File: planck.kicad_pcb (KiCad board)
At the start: 2 copper layers, 53 parts, among them J1 USB_C_Receptacle_USB2.0, K1 KEYSW, K2 KEYSW, K3 KEYSW, K4 KEYSW, SW1 SW_PUSH, U1 ATmega32U4-M, Y1 Crystal_GND24_Small

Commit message: poured fills
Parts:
- J1, K1, K2, K3, K4, TP1, TP2: moved to B.Cu
- TP10: value TestPoint -> PB5; moved to B.Cu
- TP11: value TestPoint -> PB6; moved to B.Cu
- TP12: value TestPoint -> PB7; moved to B.Cu
- TP13: value TestPoint -> PC6; moved to B.Cu
- TP14: value TestPoint -> PC7; moved to B.Cu
- TP15: value TestPoint -> PD0; moved to B.Cu
- TP16: value TestPoint -> PD1; moved to B.Cu
- TP17: value TestPoint -> PD2; moved to B.Cu
- TP18: value TestPoint -> PD3; moved to B.Cu
- TP19: value TestPoint -> PD4; moved to B.Cu
- TP20: value TestPoint -> PD6; moved to B.Cu
- TP21: value TestPoint -> PD7; moved to B.Cu
- TP22: value TestPoint -> PE6; moved to B.Cu
- TP23: value TestPoint -> PF6; moved to B.Cu
- TP24: value TestPoint -> PF7; moved to B.Cu
- TP3: value TestPoint -> AREF; moved to B.Cu
- TP4: value TestPoint -> PD5; moved to B.Cu
- TP5: value TestPoint -> PB0; moved to B.Cu
- TP6: value TestPoint -> PB1; moved to B.Cu
- TP7: value TestPoint -> PB2; moved to B.Cu
- TP8: value TestPoint -> PB3; moved to B.Cu
- TP9: value TestPoint -> PB4; moved to B.Cu
- moved D2 68.3 mm to (107.2, 132.6)
- moved K1 63.7 mm to (84.8, 101.8), turned to 180 degrees
- moved K4 63.4 mm to (104.1, 101.8), turned to 180 degrees
- moved K3 62.9 mm to (84.8, 121.2), turned to 180 degrees
- moved K2 62.6 mm to (104.1, 121.2), turned to 180 degrees
- moved D6 62.1 mm to (107.2, 111.8)
- moved C1 61.5 mm to (90.9, 95.0), turned to 90 degrees
- moved D5 60.0 mm to (86.9, 132.1)
- moved R4 57.9 mm to (107.7, 95.0), turned to 90 degrees
- moved TP13 56.1 mm to (94.5, 87.4), turned to 180 degrees
- moved TP1 55.2 mm to (99.6, 87.4), turned to 180 degrees
- moved TP23 53.6 mm to (86.9, 87.4), turned to 180 degrees
- moved C8 51.8 mm to (82.8, 81.8)
- moved SW1 51.3 mm to (84.8, 86.4)
- moved TP8 50.0 mm to (94.5, 83.3), turned to 180 degrees
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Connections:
- net /reset renamed /~{reset}
- net Net-(TP10-Pad1) renamed /PB5
- net Net-(TP11-Pad1) renamed /PB6
- net Net-(TP12-Pad1) renamed /PB7
- net Net-(TP13-Pad1) renamed /PC6
- net Net-(TP14-Pad1) renamed /PC7
- net Net-(TP15-Pad1) renamed /PD0
- net Net-(TP16-Pad1) renamed /PD1
- net Net-(TP17-Pad1) renamed /PD2
- net Net-(TP18-Pad1) renamed /PD3
- net Net-(TP19-Pad1) renamed /PD4
- net Net-(TP20-Pad1) renamed /PD6
- net Net-(TP21-Pad1) renamed /PD7
- net Net-(TP22-Pad1) renamed /PE6
- net Net-(TP23-Pad1) renamed /PF6
- net Net-(TP24-Pad1) renamed /PF7
- net Net-(TP4-Pad1) renamed /PD5
- net Net-(TP5-Pad1) renamed /PB0
- net Net-(TP6-Pad1) renamed /PB1
- net Net-(TP7-Pad1) renamed /PB2
- net Net-(TP8-Pad1) renamed /PB3
- net Net-(TP9-Pad1) renamed /PB4
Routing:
- added copper zone on B.Cu, net GND
- added copper zone on F.Cu, net GND
- added copper zone on In1.Cu, net GND
- added copper zone on In2.Cu, net VCC
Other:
- board outline added: 39.4 x 58.4 mm
- copper layers 2 -> 4

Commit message: started routing
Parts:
- moved R3 7.81 mm to (113.0, 95.5), turned to 0 degrees
- moved D4 7.44 mm to (113.5, 92.4), turned to 180 degrees
- moved D3 3.50 mm to (108.9, 92.5), turned to 0 degrees
- moved D2 1.85 mm to (106.7, 130.8)
- moved D5 1.48 mm to (87.6, 130.8)
- moved C7 1.14 mm to (81.4, 93.4)
- moved C9 1.10 mm to (87.2, 93.5)
- moved D1 0.76 mm to (87.4, 111.3)
- moved D6 0.72 mm to (106.7, 111.3)
- moved R4 0.30 mm to (107.9, 95.2), turned to 0 degrees
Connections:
- net /~{reset} renamed /~{{reset}}
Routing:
- net /col0: track 0.00 -> 27.8 mm
- net /col1: track 0.00 -> 27.3 mm
- net /row0: track 0.00 -> 21.6 mm
- net /row1: track 0.00 -> 21.5 mm
- net Net-(D4-Pad1): track 0.00 -> 8.57 mm, vias 0 -> 1
- net Net-(D2-Pad2): track 0.00 -> 8.01 mm
- net Net-(D5-Pad2): track 0.00 -> 7.90 mm
- net Net-(D1-Pad2): track 0.00 -> 7.80 mm
- net Net-(D6-Pad2): track 0.00 -> 7.80 mm
- net Net-(D3-Pad1): track 0.00 -> 5.63 mm

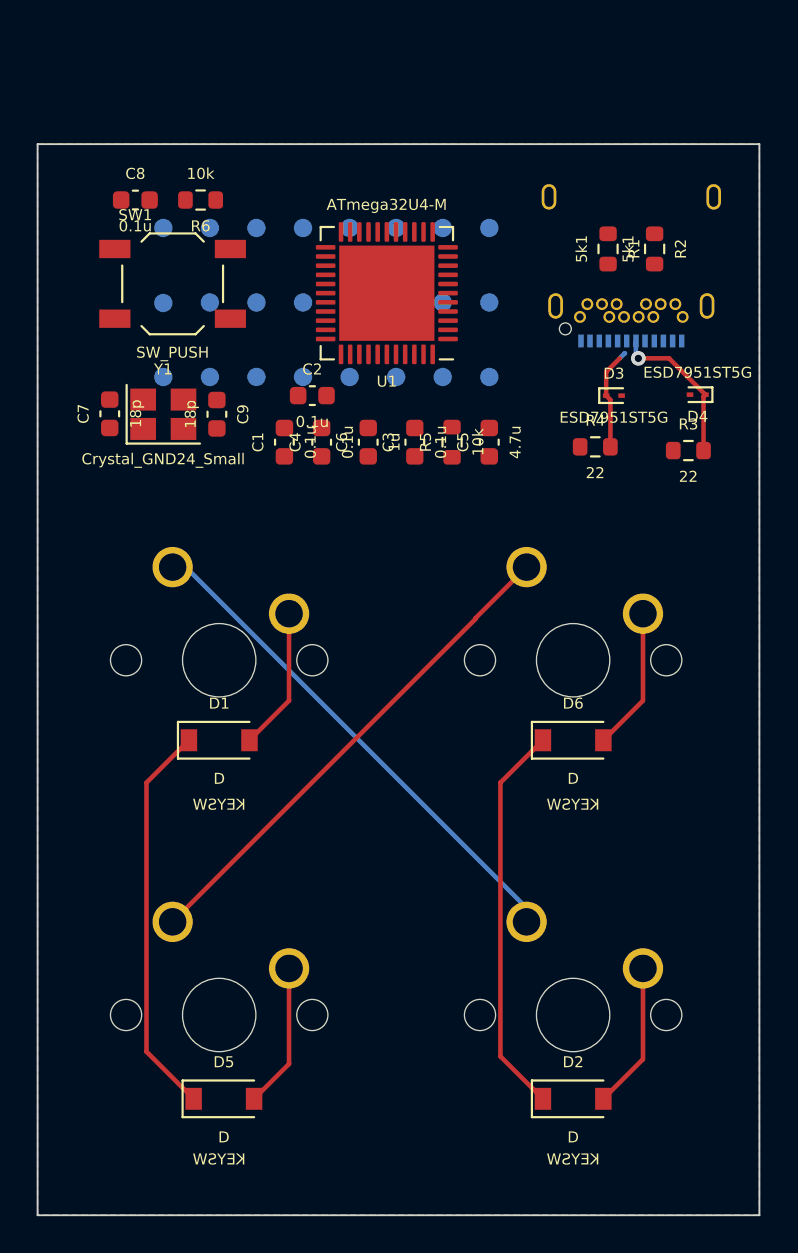
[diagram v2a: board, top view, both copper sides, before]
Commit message: routed crystal
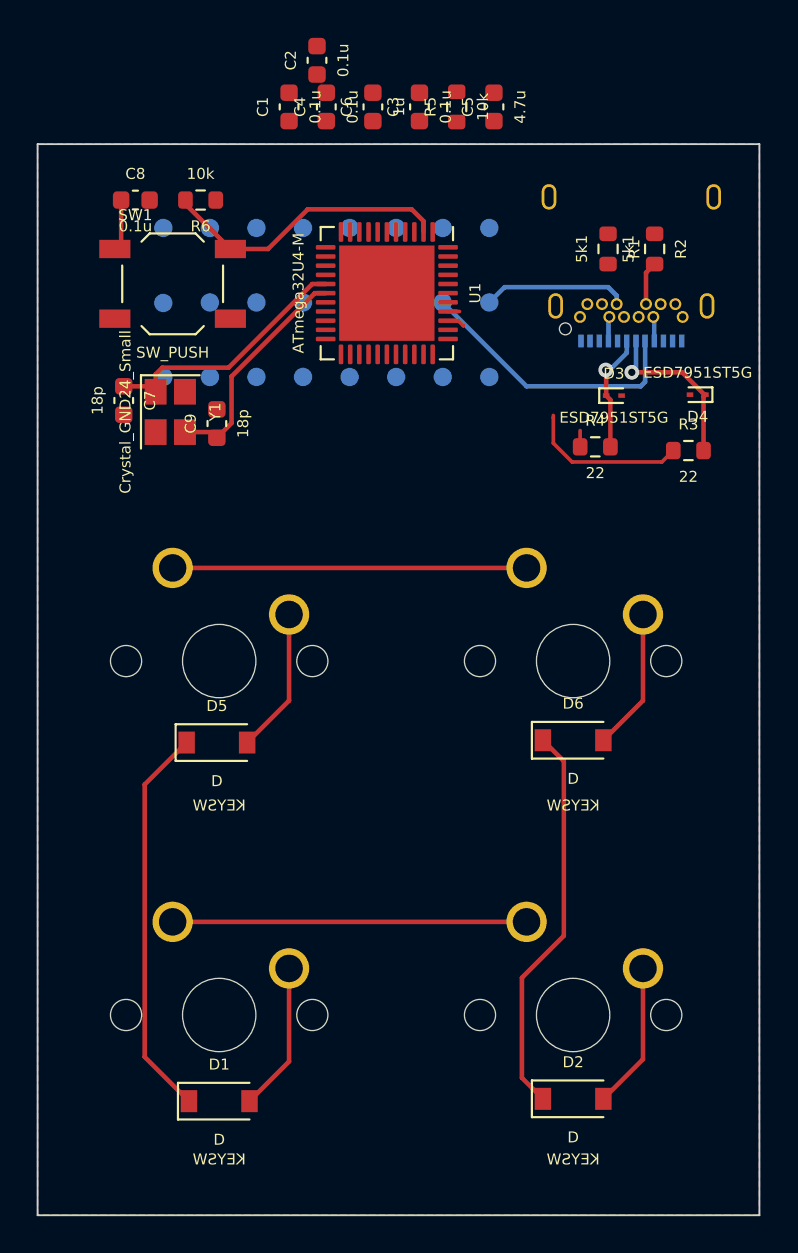
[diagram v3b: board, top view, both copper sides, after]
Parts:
- moved D1 19.7 mm to (87.4, 130.9)
- moved D5 19.4 mm to (87.2, 111.4)
- moved K1 19.3 mm to (84.8, 121.2)
- moved K3 19.3 mm to (84.8, 101.9)
- moved C1 18.3 mm to (91.2, 76.7)
- moved C2 18.3 mm to (92.7, 74.2), turned to 90 degrees
- moved C3 18.3 mm to (98.3, 76.7)
- moved C4 18.3 mm to (93.2, 76.7)
- moved C5 18.3 mm to (102.4, 76.7)
- moved C6 18.3 mm to (95.8, 76.7)
- moved R5 18.3 mm to (100.3, 76.7)
- moved TP2 5.08 mm to (102.1, 87.4)
- moved TP3 5.08 mm to (97.0, 87.4), turned to -90 degrees
- moved C7 1.05 mm to (82.2, 92.7), turned to -90 degrees
- moved C9 0.51 mm to (87.2, 94.0), turned to 90 degrees
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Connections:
- net /~{{reset}} renamed /~reset
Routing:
- net /~reset: track 0.00 -> 18.8 mm
- net Net-(J1-PadA8): track 0.00 -> 15.3 mm
- net /XTAL2: track 0.00 -> 14.2 mm
- net /XTAL1: track 0.00 -> 12.6 mm
- net /D-: track 0.00 -> 8.74 mm
- net Net-(J1-PadB8): track 0.00 -> 7.95 mm
- net /col0: track 27.8 -> 20.1 mm
- net /col1: track 27.3 -> 20.0 mm
- net VCC: track 0.00 -> 2.66 mm
- net Net-(J1-PadB5): track 0.00 -> 2.38 mm
- net /PF7: track 0.00 -> 0.97 mm
- net /D+: track 0.00 -> 0.89 mm
- net Net-(D3-Pad1): track 5.63 -> 6.48 mm, vias 0 -> 1
- net Net-(D4-Pad1): track 8.57 -> 9.41 mm
- net /PF6: track 0.00 -> 0.63 mm

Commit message: finishing it off
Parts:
- removed TP10: PB5, TestPoint:TestPoint_Pad_D1.0mm
- removed TP11: PB6, TestPoint:TestPoint_Pad_D1.0mm
- removed TP12: PB7, TestPoint:TestPoint_Pad_D1.0mm
- removed TP13: PC6, TestPoint:TestPoint_Pad_D1.0mm
- removed TP14: PC7, TestPoint:TestPoint_Pad_D1.0mm
- removed TP15: PD0, TestPoint:TestPoint_Pad_D1.0mm
- removed TP16: PD1, TestPoint:TestPoint_Pad_D1.0mm
- removed TP17: PD2, TestPoint:TestPoint_Pad_D1.0mm
- removed TP18: PD3, TestPoint:TestPoint_Pad_D1.0mm
- removed TP19: PD4, TestPoint:TestPoint_Pad_D1.0mm
- removed TP20: PD6, TestPoint:TestPoint_Pad_D1.0mm
- removed TP21: PD7, TestPoint:TestPoint_Pad_D1.0mm
- removed TP22: PE6, TestPoint:TestPoint_Pad_D1.0mm
- removed TP23: PF6, TestPoint:TestPoint_Pad_D1.0mm
- removed TP24: PF7, TestPoint:TestPoint_Pad_D1.0mm
- removed TP4: PD5, TestPoint:TestPoint_Pad_D1.0mm
- removed TP5: PB0, TestPoint:TestPoint_Pad_D1.0mm
- removed TP6: PB1, TestPoint:TestPoint_Pad_D1.0mm
- removed TP7: PB2, TestPoint:TestPoint_Pad_D1.0mm
- removed TP8: PB3, TestPoint:TestPoint_Pad_D1.0mm
- removed TP9: PB4, TestPoint:TestPoint_Pad_D1.0mm
- moved TP3 31.4 mm to (121.4, 67.6)
- moved TP1 29.0 mm to (123.4, 70.9)
- moved TP2 29.0 mm to (126.0, 70.9)
- moved R5 25.7 mm to (80.2, 92.6), turned to 180 degrees
- moved C7 24.0 mm to (63.5, 77.6)
- moved C9 24.0 mm to (68.6, 78.9)
- moved Y1 24.0 mm to (66.0, 78.2)
- moved C3 20.4 mm to (89.2, 94.9), turned to -90 degrees
- moved C1 20.2 mm to (82.4, 94.9), turned to -90 degrees
- moved C2 17.1 mm to (80.2, 85.9), turned to 180 degrees
- moved SW1 16.7 mm to (96.8, 74.7), turned to 90 degrees
- moved C5 16.5 mm to (87.3, 83.5)
- moved C4 14.6 mm to (91.5, 91.2), turned to 0 degrees
- moved C6 13.2 mm to (91.5, 89.2), turned to 0 degrees
- moved U1 10.9 mm to (85.8, 89.2), turned to 180 degrees
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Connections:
- U1 pad 1: /PE6 -> unconnected-(U1-Pad1)
- U1 pad 10: /PB2 -> unconnected-(U1-Pad10)
- U1 pad 11: /PB3 -> unconnected-(U1-Pad11)
- U1 pad 12: /PB7 -> unconnected-(U1-Pad12)
- U1 pad 18: /PD0 -> unconnected-(U1-Pad18)
- U1 pad 19: /PD1 -> unconnected-(U1-Pad19)
- U1 pad 20: /PD2 -> unconnected-(U1-Pad20)
- U1 pad 21: /PD3 -> unconnected-(U1-Pad21)
- U1 pad 22: /PD5 -> unconnected-(U1-Pad22)
- U1 pad 25: /PD4 -> unconnected-(U1-Pad25)
- U1 pad 26: /PD6 -> unconnected-(U1-Pad26)
- U1 pad 27: /PD7 -> unconnected-(U1-Pad27)
- U1 pad 28: /PB4 -> unconnected-(U1-Pad28)
- U1 pad 29: /PB5 -> unconnected-(U1-Pad29)
- U1 pad 30: /PB6 -> unconnected-(U1-Pad30)
- U1 pad 31: /PC6 -> unconnected-(U1-Pad31)
- U1 pad 32: /PC7 -> unconnected-(U1-Pad32)
- U1 pad 36: /PF7 -> unconnected-(U1-Pad36)
- U1 pad 37: /PF6 -> unconnected-(U1-Pad37)
- U1 pad 8: /PB0 -> unconnected-(U1-Pad8)
- U1 pad 9: /PB1 -> unconnected-(U1-Pad9)
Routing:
- net VCC: track 2.66 -> 20.7 mm, vias 0 -> 6
- net /XTAL2: track 14.2 -> 0.00 mm
- net Net-(J1-PadA8): track 15.3 -> 2.57 mm
- net /XTAL1: track 12.6 -> 0.00 mm
- net /~reset: track 18.8 -> 7.85 mm
- net Net-(J1-PadB8): track 7.95 -> 1.12 mm
- net Net-(R5-Pad1): track 0.00 -> 1.89 mm
- net Net-(C6-Pad1): track 0.00 -> 1.56 mm
- net /PF7: track 0.97 -> 0.00 mm
- net /PF6: track 0.63 -> 0.00 mm
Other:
- board size 39.4 x 58.4 mm -> 76.6 x 75.1 mm

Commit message: switched pins for switches
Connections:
- U1 pad 38: /col1 -> /row0
- U1 pad 40: /row1 -> /col1
- U1 pad 41: /row0 -> /row1
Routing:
- net /row1: track 21.5 -> 53.1 mm
- net /col0: track 20.1 -> 46.5 mm
- net /row0: track 21.5 -> 37.3 mm
- net /col1: track 20.0 -> 24.3 mm

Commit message: finished layout
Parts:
- J1, TP1, TP2: moved to F.Cu
- moved TP3 62.6 mm to (85.0, 118.5), turned to 180 degrees
- moved TP2 54.4 mm to (110.5, 123.0), turned to 90 degrees
- moved C7 52.0 mm to (100.3, 114.4), turned to 42.5 degrees
- moved SW1 50.7 mm to (97.0, 125.4), turned to 0 degrees
- moved R6 48.9 mm to (99.1, 121.6), turned to 0 degrees
- moved TP1 47.7 mm to (104.0, 114.4), turned to -90 degrees
- moved Y1 47.3 mm to (99.0, 112.1), turned to 42.5 degrees
- moved C9 45.2 mm to (101.2, 110.2), turned to -47.5 degrees
- moved C8 44.9 mm to (95.2, 121.6), turned to 0 degrees
- moved R2 38.9 mm to (114.2, 123.2), turned to 180 degrees
- moved R1 38.4 mm to (106.2, 122.8), turned to 180 degrees
- moved C5 36.0 mm to (96.8, 118.3), turned to 0 degrees
- moved C6 33.4 mm to (91.9, 122.6), turned to -90 degrees
- moved J1 32.1 mm to (110.9, 116.6), turned to 90 degrees
- moved C4 31.2 mm to (88.3, 122.2), turned to -90 degrees
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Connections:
- U1 pad 38: /row0 -> /col1
- U1 pad 39: /col0 -> /row0
- U1 pad 40: /col1 -> /col0
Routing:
- net /D+: track 0.89 -> 24.2 mm
- net /row1: track 53.1 -> 76.1 mm
- net GND: track 0.30 -> 21.6 mm, vias 0 -> 1
- net /D-: track 8.74 -> 24.6 mm
- net /col1: track 24.3 -> 36.9 mm
- net /XTAL1: track 0.00 -> 11.4 mm
- net /row0: track 37.3 -> 46.0 mm
- net /XTAL2: track 0.00 -> 7.94 mm
- net Net-(J1-PadB5): track 2.38 -> 9.68 mm
- net /~reset: track 7.85 -> 14.4 mm
- net Net-(J1-PadA5): track 0.00 -> 6.24 mm
- net Net-(J1-PadB8): track 1.12 -> 7.01 mm
- net Net-(D1-Pad2): track 8.13 -> 2.98 mm
- net Net-(D5-Pad2): track 7.93 -> 2.79 mm
- net Net-(D6-Pad2): track 7.80 -> 2.90 mm
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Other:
- board size 76.6 x 75.1 mm -> 38.8 x 39.8 mm

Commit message: finished layout
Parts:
- TP3: moved to F.Cu
- moved TP2 7.08 mm to (103.4, 123.2), turned to 0 degrees
- moved R2 4.28 mm to (110.0, 123.9), turned to 45 degrees
- moved C9 3.96 mm to (97.5, 111.5), turned to 0 degrees
- moved R1 3.24 mm to (104.2, 120.3), turned to 90 degrees
- moved Y1 2.82 mm to (97.4, 114.5), turned to 90 degrees
- moved C2 1.39 mm to (93.0, 111.5), turned to 180 degrees
- moved R5 1.14 mm to (88.3, 111.5), turned to 0 degrees
- moved TP1 1.10 mm to (103.0, 114.0)
- moved C7 0.73 mm to (100.0, 115.1), turned to 90 degrees
- turned TP3 to 0 degrees
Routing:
- net Net-(J1-PadB8): track 7.01 -> 11.7 mm
- net /XTAL1: track 11.4 -> 6.88 mm
- net Net-(J1-PadA5): track 6.24 -> 3.25 mm
- net /row1: track 76.1 -> 74.8 mm
- net Net-(J1-PadA8): track 2.51 -> 3.70 mm
- net /XTAL2: track 7.94 -> 6.77 mm
- net Net-(J1-PadB5): track 9.68 -> 8.90 mm

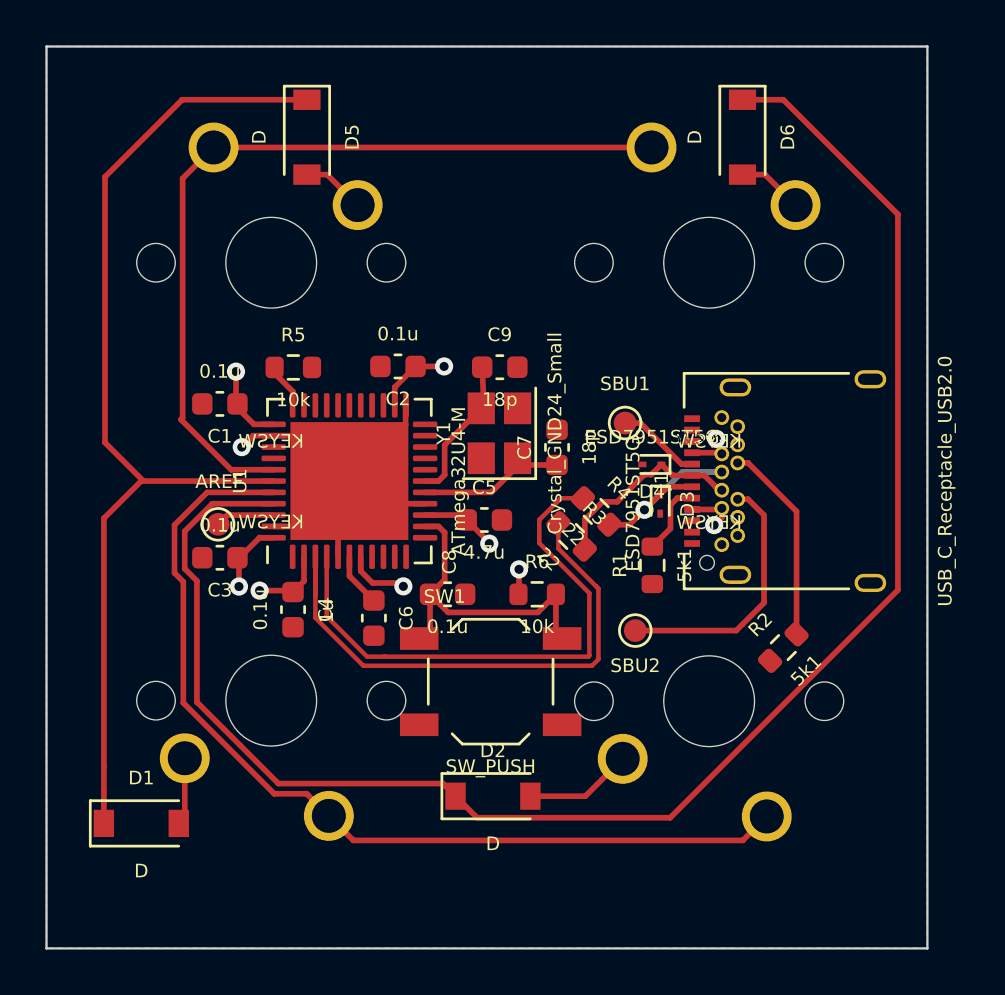
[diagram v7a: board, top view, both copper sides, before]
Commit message: added digikey library
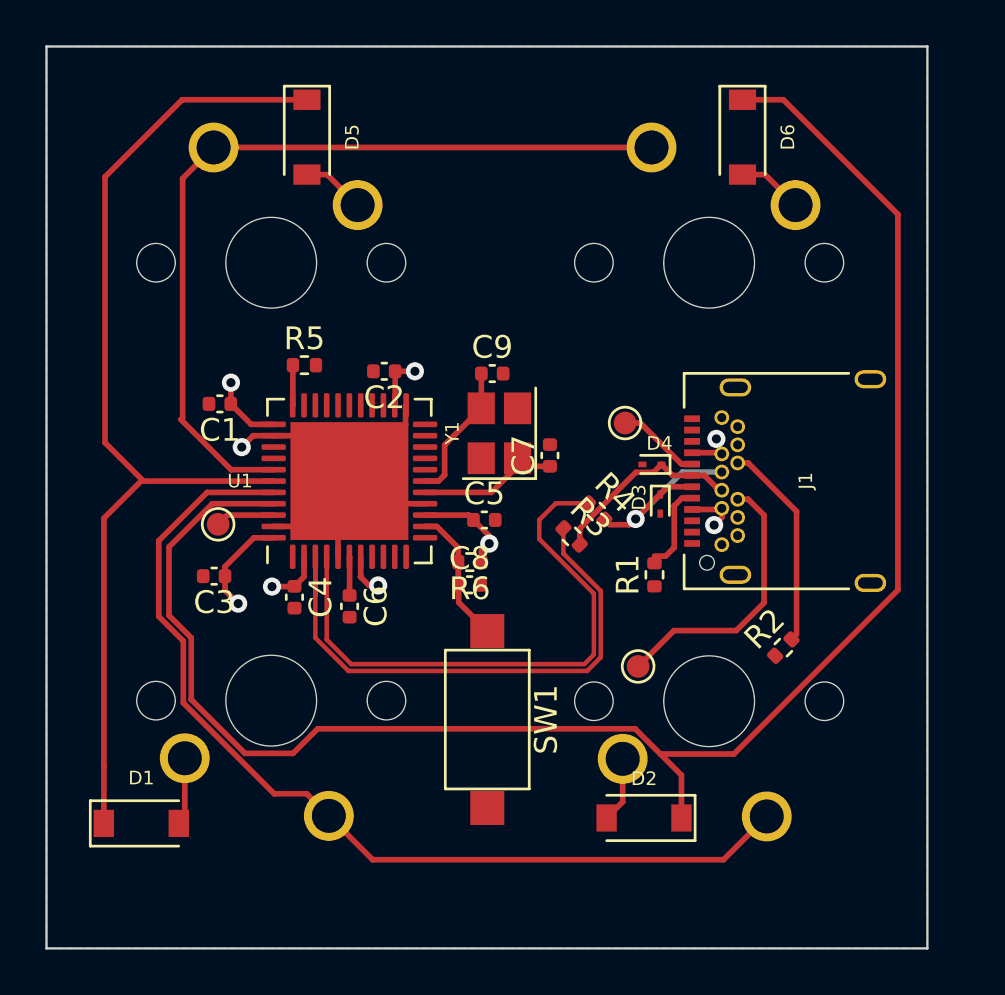
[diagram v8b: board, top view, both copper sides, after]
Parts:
- C1, C2, C3, C4, C5, C6, C7, C8, C9: footprint Capacitor_SMD:C_0603_1608Metric -> Capacitor_SMD:C_0402_1005Metric
- R1, R2, R3, R4, R5, R6: footprint Resistor_SMD:R_0603_1608Metric -> Resistor_SMD:R_0402_1005Metric
- SW1: footprint Button_Switch_SMD:SW_SPST_TL3342 -> Button_Switch_SMD:SW_SPST_CK_RS282G05A3
- moved D2 6.73 mm to (103.8, 131.4), turned to 180 degrees
- moved R6 3.29 mm to (96.1, 120.1), turned to 180 degrees
- moved SW1 1.68 mm to (96.9, 127.1), turned to -90 degrees
- moved TP2 1.58 mm to (103.5, 124.7)
- moved C6 1.19 mm to (90.8, 122.1)
- moved C8 1.06 mm to (96.1, 121.1)
- moved C3 0.85 mm to (84.9, 120.8)
- moved C2 0.64 mm to (92.4, 111.7)
- moved C4 0.55 mm to (88.4, 121.7)
- moved R5 0.50 mm to (88.8, 111.5)
- moved C7 0.47 mm to (99.7, 115.4)
- moved C9 0.43 mm to (97.1, 111.8)
- moved R1 0.43 mm to (104.3, 120.7)
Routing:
- net /~reset: track 14.4 -> 6.05 mm
- net /row1: track 74.8 -> 77.3 mm
- net VCC: track 24.4 -> 22.4 mm, vias 9 -> 8
- net Net-(D2-Pad2): track 4.75 -> 2.90 mm
- net /col0: track 41.6 -> 42.9 mm
- net /D+: track 24.2 -> 25.4 mm
- net /XTAL1: track 6.88 -> 6.11 mm
- net Net-(C6-Pad1): track 2.38 -> 1.71 mm
- net Net-(D3-Pad1): track 8.44 -> 8.99 mm
- net Net-(J1-PadA5): track 3.25 -> 3.79 mm
- net Net-(J1-PadB8): track 11.7 -> 12.2 mm
